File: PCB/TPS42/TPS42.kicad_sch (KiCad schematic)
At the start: 83 parts, among them J1 PJ-320A, J10 TP Module, J11 Conn_01x09, J12 Conn_01x09, J13 Conn_01x09, J14 FH12-10S-0.5SH, J2 Conn_01x09, J3 TP Sensor Module, J4 TP Module, J5 TrackPoint, J6 OLED, J7 TrackPoint, J8 Battery, J9 TP Sensor Module, SW1 SW_DPST_x2, SW2 Reset, U1 ProMicro, U10 Hole, U11 Hole, U12 Hole, U14 ProMicro, U2 Hole, U3 Hole, U4 Hole, U5 Hole, U6 Hole, U7 Hole, U8 Hole, U9 Hole

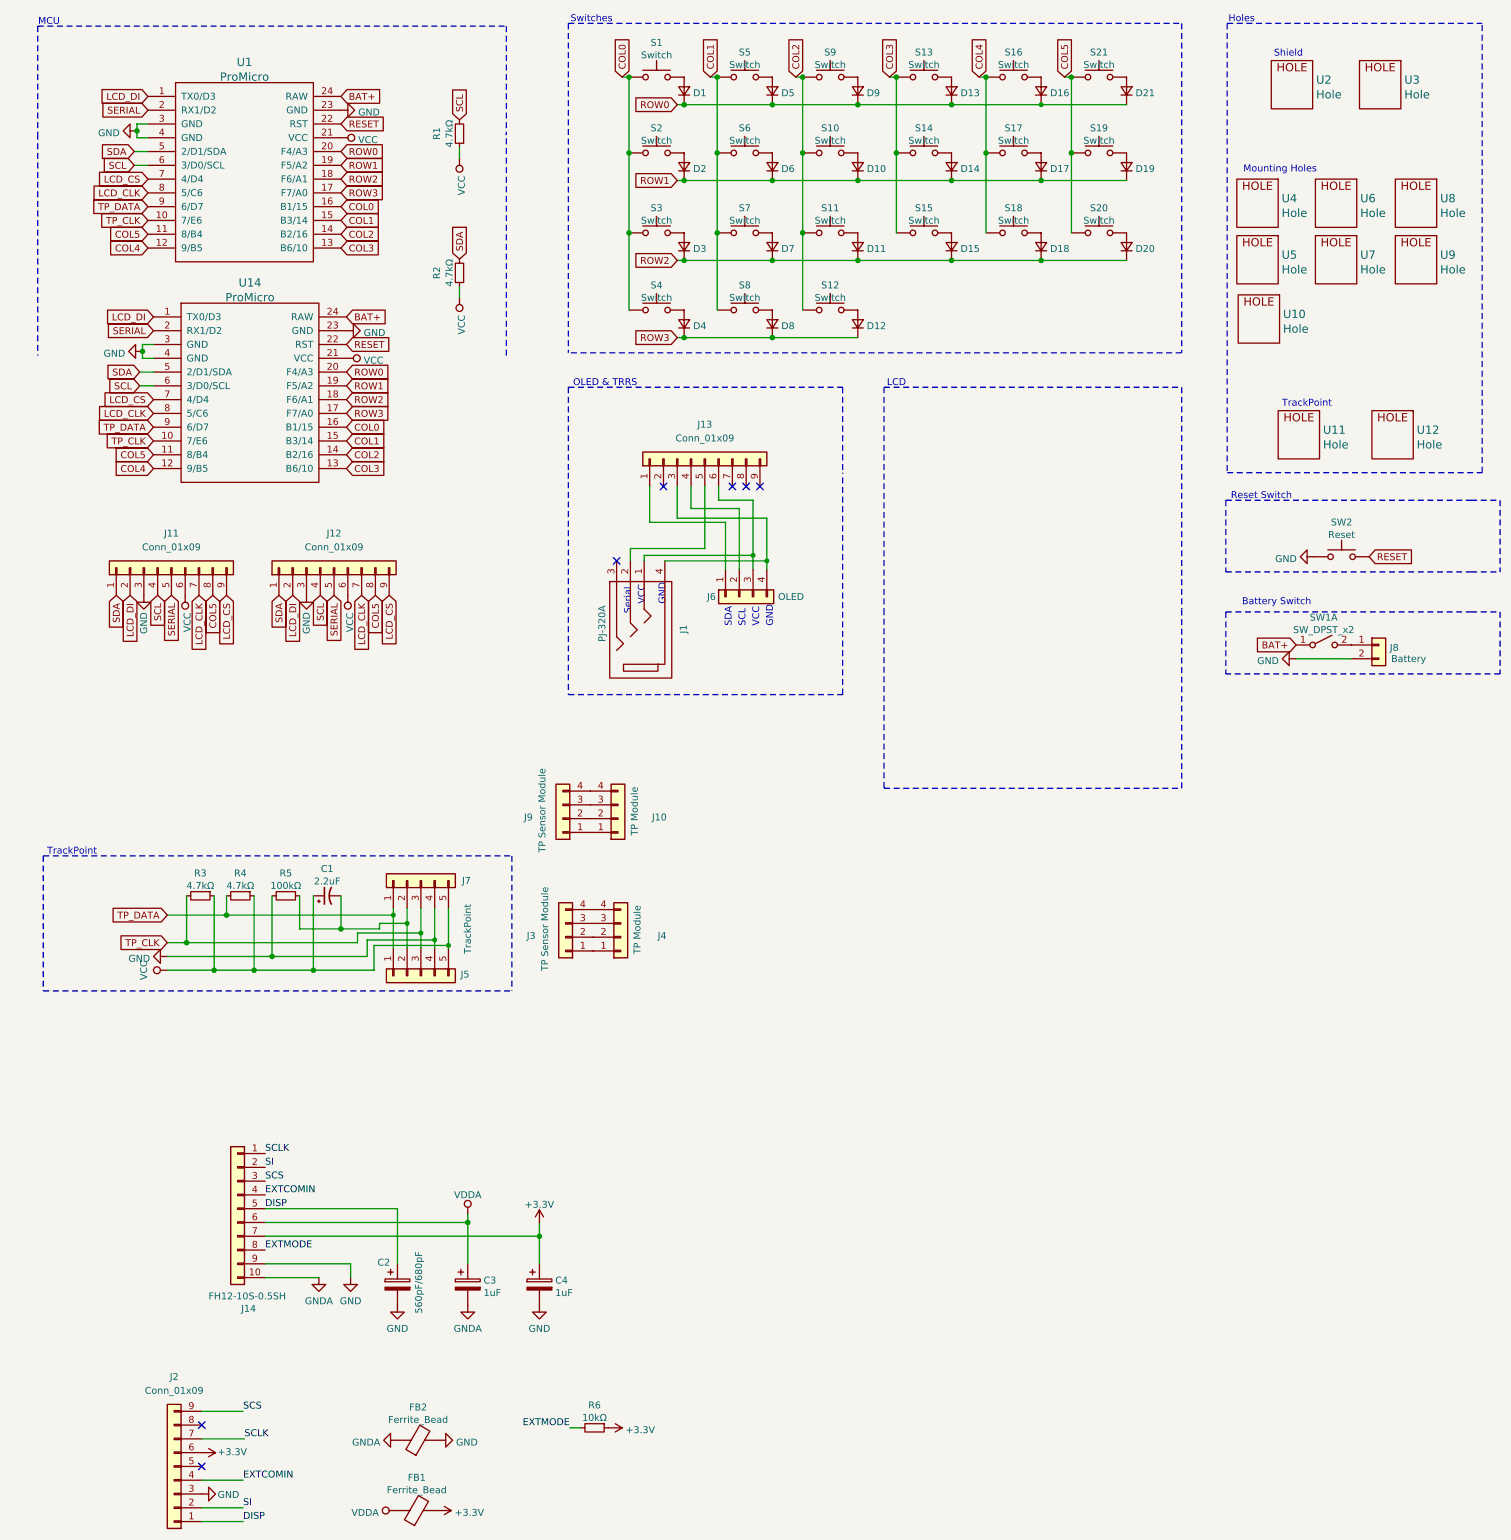
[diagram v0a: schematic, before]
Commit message: align footprints
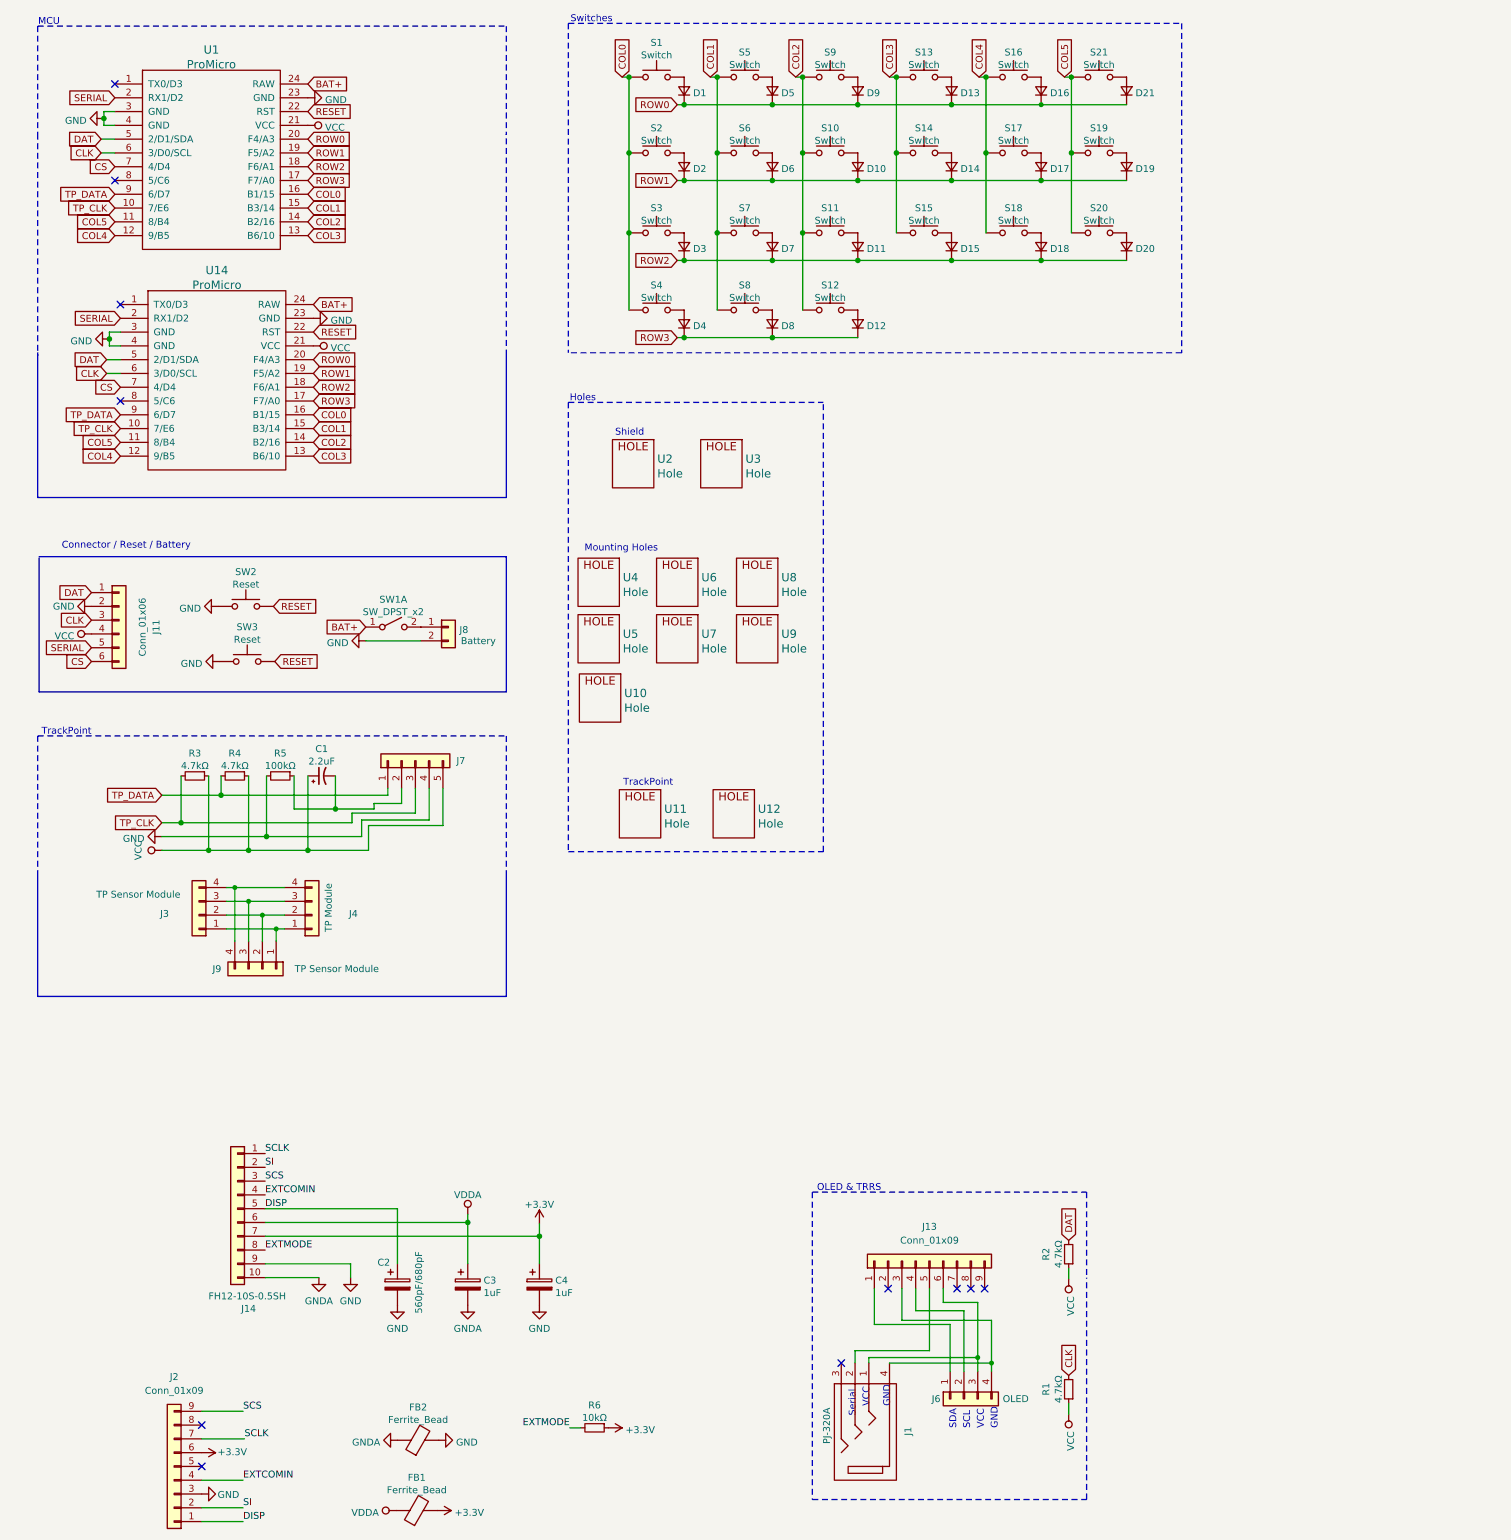
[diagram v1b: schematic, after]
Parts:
- removed J10: TP Module, TPS42:TPSensorModule_Connector, symbol Connector_Generic:Conn_01x04
- removed J11: Conn_01x09, TPS42:Connector_Reversable_3x3_A, symbol Connector_Generic:Conn_01x09
- removed J12: Conn_01x09, TPS42:Connector_Reversable_3x3_B, symbol Connector_Generic:Conn_01x09
- removed J5: TrackPoint, TPS42:TPModule, symbol Connector_Generic:Conn_01x05
- added J11: Conn_01x06, Connector_PinHeader_2.54mm:PinHeader_2x03_P2.54mm_Vertical, symbol Connector_Generic:Conn_01x06
- added SW3: Reset, TPS42:SMD-SW-4_5.1x5.1x2.5, symbol Switch:SW_Push
- S12, S5, S6: footprint TPS42:SW_PG1350_reversible -> TPS42:Kailh_socket_PG1350_optional_reversible.kicad_mod
- SW2: footprint TPS42:SW_Tactile_SPST_Angled_PTS645Vx39-2LFS -> TPS42:SMD-SW-4_5.1x5.1x2.5
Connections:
- net GND: now also J11.2 (Pin_2), SW3.1
- net RESET: now also SW3.2
- net SERIAL: now also J11.5 (Pin_5)
- net VCC: now also J11.4 (Pin_4)
- net at J3.1 (Pin_1), J4.1 (Pin_1): now also J9.1 (Pin_1)
- net at J3.2 (Pin_2), J4.2 (Pin_2): now also J9.2 (Pin_2)
- net at J3.3 (Pin_3), J4.3 (Pin_3): now also J9.3 (Pin_3)
- net at J3.4 (Pin_4), J4.4 (Pin_4): now also J9.4 (Pin_4)
- net LCD_CLK: no longer names the net of U1.8 (5/C6)
- net LCD_CLK: no longer U14.8 (5/C6)
- net LCD_CS renamed CS
- net CS: now also J11.6 (Pin_6)
- net LCD_DI: no longer names the net of U1.1 (TX0/D3)
- net LCD_DI: no longer U14.1 (TX0/D3)
- net SCL renamed CLK
- net CLK: now also J11.3 (Pin_3)
- net SDA renamed DAT
- net DAT: now also J11.1 (Pin_1)
- no-connect marks 7 -> 11
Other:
- note added: "Connector / Reset / Battery"
- note removed: "Battery Switch"
- note removed: "LCD"
- note removed: "Reset Switch"
- moved on the sheet: C1, J1, J13, J3, J4, J6, J7, J8, J9, R1, R2, R3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

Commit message: Further footprint changes
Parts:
- C1: footprint TPS42:C_THT_SMD_0805_HandSolder_Reversable -> TPS42:C_0603_1608Metric_Pad1.08x0.95mm_HandSolder_Reversable
- C2, C3, C4: footprint Capacitor_SMD:C_0603_1608Metric_Pad1.08x0.95mm_HandSolder -> TPS42:C_0603_1608Metric_Pad1.08x0.95mm_HandSolder_Reversable
- R1, R2, R3, R4, R5: footprint TPS42:Resistor-TH_SMD -> TPS42:R_0603_1608Metric_Pad0.98x0.95mm_HandSolder_Reversable
- R6: footprint Resistor_SMD:R_0603_1608Metric_Pad0.98x0.95mm_HandSolder -> TPS42:R_0603_1608Metric_Pad0.98x0.95mm_HandSolder_Reversable
- S6: footprint TPS42:Kailh_socket_PG1350_optional_reversible.kicad_mod -> TPS42:SW_PG1350_reversible
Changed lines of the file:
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@@
     (property "Reference" "R4" (id 0) (at 51.816 150.7702 90))
     (property "Value" "4.7kΩ" (id 1) (at 51.816 153.0689 90))
-    (property "Footprint" "TPS42:Resistor-TH_SMD" (id 2) (at 51.816 154.94 0)
+    (property "Footprint" "TPS42:R_0603_1608Metric_Pad0.98x0.95mm_HandSolder_Reversable" (id 2) (at 51.816 154.94 0)
       (effects (font (size 1.27 1.27)) hide)
     )
@@
       (effects (font (size 1.27 1.27)) (justify left))
     )
-    (property "Footprint" "Capacitor_SMD:C_0603_1608Metric_Pad1.08x0.95mm_HandSolder" (id 2) (at 82.7532 252.476 0)
+    (property "Footprint" "TPS42:C_0603_1608Metric_Pad1.08x0.95mm_HandSolder_Reversable" (id 2) (at 82.7532 252.476 0)
       (effects (font (size 1.27 1.27)) hide)
     )
@@
     (property "Reference" "R5" (id 0) (at 60.198 150.7702 90))
     (property "Value" "100kΩ" (id 1) (at 60.198 153.0689 90))
-    (property "Footprint" "TPS42:Resistor-TH_SMD" (id 2) (at 60.198 154.94 0)
+    (property "Footprint" "TPS42:R_0603_1608Metric_Pad0.98x0.95mm_HandSolder_Reversable" (id 2) (at 60.198 154.94 0)
       (effects (font (size 1.27 1.27)) hide)
     )
@@
     (property "Reference" "R2" (id 0) (at 201.3162 243.078 90))
     (property "Value" "4.7kΩ" (id 1) (at 203.6149 243.078 90))
-    (property "Footprint" "TPS42:Resistor-TH_SMD" (id 2) (at 205.486 243.078 0)
+    (property "Footprint" "TPS42:R_0603_1608Metric_Pad0.98x0.95mm_HandSolder_Reversable" (id 2) (at 205.486 243.078 0)
       (effects (font (size 1.27 1.27)) hide)
     )
@@
       (effects (font (size 1.27 1.27)) (justify left))
     )
-    (property "Footprint" "Capacitor_SMD:C_0603_1608Metric_Pad1.08x0.95mm_HandSolder" (id 2) (at 108.9152 252.476 0)
+    (property "Footprint" "TPS42:C_0603_1608Metric_Pad1.08x0.95mm_HandSolder_Reversable" (id 2) (at 108.9152 252.476 0)
       (effects (font (size 1.27 1.27)) hide)
     )
@@
     (property "Reference" "R6" (id 0) (at 118.11 270.9122 90))
     (property "Value" "10kΩ" (id 1) (at 118.11 273.2109 90))
-    (property "Footprint" "Resistor_SMD:R_0603_1608Metric_Pad0.98x0.95mm_HandSolder" (id 2) (at 118.11 275.082 0)
+    (property "Footprint" "TPS42:R_0603_1608Metric_Pad0.98x0.95mm_HandSolder_Reversable" (id 2) (at 118.11 275.082 0)
       (effects (font (size 1.27 1.27)) hide)
     )
@@
     (property "Reference" "C1" (id 0) (at 67.818 149.9574 90))
     (property "Value" "2.2uF" (id 1) (at 67.818 152.2561 90))
-    (property "Footprint" "TPS42:C_THT_SMD_0805_HandSolder_Reversable" (id 2) (at 67.818 154.94 0)
+    (property "Footprint" "TPS42:C_0603_1608Metric_Pad1.08x0.95mm_HandSolder_Reversable" (id 2) (at 67.818 154.94 0)
       (effects (font (size 1.27 1.27)) hide)
     )
@@
     (property "Reference" "S6" (id 0) (at 145.796 35.5558 0))
     (property "Value" "Switch" (id 1) (at 145.796 37.8545 0))
-    (property "Footprint" "TPS42:Kailh_socket_PG1350_optional_reversible.kicad_mod" (id 2) (at 145.796 35.052 0)
+    (property "Footprint" "TPS42:SW_PG1350_reversible" (id 2) (at 145.796 35.052 0)
       (effects (font (size 1.27 1.27)) hide)
     )
@@
     (property "Reference" "R3" (id 0) (at 44.45 150.7702 90))
     (property "Value" "4.7kΩ" (id 1) (at 44.45 153.0689 90))
-    (property "Footprint" "TPS42:Resistor-TH_SMD" (id 2) (at 44.45 154.94 0)
+    (property "Footprint" "TPS42:R_0603_1608Metric_Pad0.98x0.95mm_HandSolder_Reversable" (id 2) (at 44.45 154.94 0)
       (effects (font (size 1.27 1.27)) hide)
     )
@@
       (effects (font (size 1.27 1.27)) (justify left))
     )
-    (property "Footprint" "Capacitor_SMD:C_0603_1608Metric_Pad1.08x0.95mm_HandSolder" (id 2) (at 95.7072 252.476 0)
+    (property "Footprint" "TPS42:C_0603_1608Metric_Pad1.08x0.95mm_HandSolder_Reversable" (id 2) (at 95.7072 252.476 0)
       (effects (font (size 1.27 1.27)) hide)
     )
@@
     (property "Reference" "R1" (id 0) (at 201.3162 267.97 90))
     (property "Value" "4.7kΩ" (id 1) (at 203.6149 267.97 90))
-    (property "Footprint" "TPS42:Resistor-TH_SMD" (id 2) (at 205.486 267.97 0)
+    (property "Footprint" "TPS42:R_0603_1608Metric_Pad0.98x0.95mm_HandSolder_Reversable" (id 2) (at 205.486 267.97 0)
       (effects (font (size 1.27 1.27)) hide)
     )
@@
     )
     (path "/c869f587-3433-4e49-b864-4e64391cc97e"
-      (reference "C1") (unit 1) (value "2.2uF") (footprint "TPS42:C_THT_SMD_0805_HandSolder_Reversable")
+      (reference "C1") (unit 1) (value "2.2uF") (footprint "TPS42:C_0603_1608Metric_Pad1.08x0.95mm_HandSolder_Reversable")
     )
     (path "/3a02cedd-724f-40d8-bbef-61e3b75cada0"
-      (reference "C2") (unit 1) (value "560pF/680pF") (footprint "Capacitor_SMD:C_0603_1608Metric_Pad1.08x0.95mm_HandSolder")
+      (reference "C2") (unit 1) (value "560pF/680pF") (footprint "TPS42:C_0603_1608Metric_Pad1.08x0.95mm_HandSolder_Reversable")
     )
     (path "/e6ce6c79-9170-4ea2-b9bd-87d942d1f8ee"
-      (reference "C3") (unit 1) (value "1uF") (footprint "Capacitor_SMD:C_0603_1608Metric_Pad1.08x0.95mm_HandSolder")
+      (reference "C3") (unit 1) (value "1uF") (footprint "TPS42:C_0603_1608Metric_Pad1.08x0.95mm_HandSolder_Reversable")
     )
     (path "/a3c7a0be-f018-44c9-b3c2-73fbc0d13b4a"
-      (reference "C4") (unit 1) (value "1uF") (footprint "Capacitor_SMD:C_0603_1608Metric_Pad1.08x0.95mm_HandSolder")
+      (reference "C4") (unit 1) (value "1uF") (footprint "TPS42:C_0603_1608Metric_Pad1.08x0.95mm_HandSolder_Reversable")
     )
     (path "/f30d5869-ca91-43cc-a29d-95c683eebd02"
@@
     )
     (path "/ea395e03-04fd-4d87-bca2-a4cd85afd730"
-      (reference "R1") (unit 1) (value "4.7kΩ") (footprint "TPS42:Resistor-TH_SMD")
+      (reference "R1") (unit 1) (value "4.7kΩ") (footprint "TPS42:R_0603_1608Metric_Pad0.98x0.95mm_HandSolder_Reversable")
     )
     (path "/9a947dc8-1f6d-4a7b-b627-92743d8030bd"
-      (reference "R2") (unit 1) (value "4.7kΩ") (footprint "TPS42:Resistor-TH_SMD")
+      (reference "R2") (unit 1) (value "4.7kΩ") (footprint "TPS42:R_0603_1608Metric_Pad0.98x0.95mm_HandSolder_Reversable")
     )
     (path "/e544431e-d006-4617-b3e5-b0c7cee368d3"
-      (reference "R3") (unit 1) (value "4.7kΩ") (footprint "TPS42:Resistor-TH_SMD")
+      (reference "R3") (unit 1) (value "4.7kΩ") (footprint "TPS42:R_0603_1608Metric_Pad0.98x0.95mm_HandSolder_Reversable")
     )
     (path "/0466771e-dbcc-4777-ba4a-e86665985a09"
-      (reference "R4") (unit 1) (value "4.7kΩ") (footprint "TPS42:Resistor-TH_SMD")
+      (reference "R4") (unit 1) (value "4.7kΩ") (footprint "TPS42:R_0603_1608Metric_Pad0.98x0.95mm_HandSolder_Reversable")
     )
     (path "/726e3017-0840-4260-a171-31d40b851a8f"
-      (reference "R5") (unit 1) (value "100kΩ") (footprint "TPS42:Resistor-TH_SMD")
+      (reference "R5") (unit 1) (value "100kΩ") (footprint "TPS42:R_0603_1608Metric_Pad0.98x0.95mm_HandSolder_Reversable")
     )
     (path "/bf76e491-9dd7-40e2-950e-c79b71b72d93"
-      (reference "R6") (unit 1) (value "10kΩ") (footprint "Resistor_SMD:R_0603_1608Metric_Pad0.98x0.95mm_HandSolder")
+      (reference "R6") (unit 1) (value "10kΩ") (footprint "TPS42:R_0603_1608Metric_Pad0.98x0.95mm_HandSolder_Reversable")
     )
     (path "/9cdf4502-752b-4f55-b9dd-3b2cc7b72863"
@@
     )
     (path "/caecacf4-cc4d-41e2-b156-a7301cb858f8"
-      (reference "S6") (unit 1) (value "Switch") (footprint "TPS42:Kailh_socket_PG1350_optional_reversible.kicad_mod")
+      (reference "S6") (unit 1) (value "Switch") (footprint "TPS42:SW_PG1350_reversible")
     )
     (path "/13477fde-7f3f-473f-a644-65c174cf4bad"

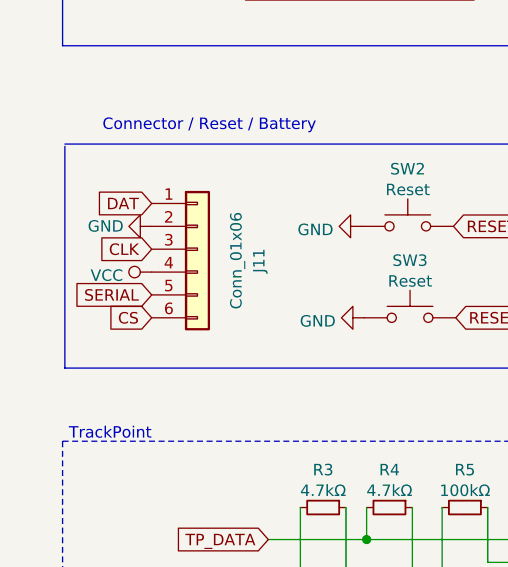
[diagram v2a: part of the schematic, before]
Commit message: replaced diode footprint
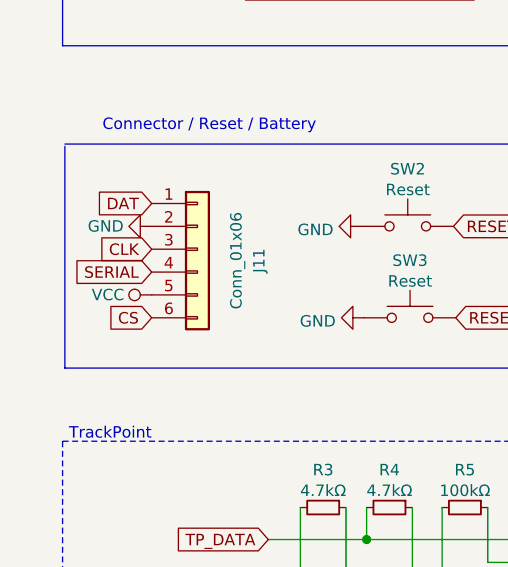
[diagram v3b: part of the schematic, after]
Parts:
- D1, D10, D11, D12, D13, D14, D15, D16, D17, D18, D19, D2, D20, D21, D3, D4, D5, D6, D7, D8, D9: footprint TPS42:D3_TH_SMD_v2 -> TPS42:D_SOD-323_HandSoldering_Reversable
- J8: footprint Connector_JST:JST_PH_S2B-PH-K_1x02_P2.00mm_Horizontal -> Connector_PinHeader_2.54mm:PinHeader_1x02_P2.54mm_Vertical
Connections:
- net SERIAL: now also J11.4 (Pin_4); no longer J11.5 (Pin_5)
- net VCC: now also J11.5 (Pin_5); no longer J11.4 (Pin_4)
